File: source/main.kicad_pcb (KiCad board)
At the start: 4 copper layers, 38 x 75 mm, 63 parts, among them J1 pf_533984002, J2 B4B_ZR_SM4_TF, J3 QWIIC, J4 USB_Type_C_Receptacle_14_pin_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, Q1 MOSFET, U1 SCD40, U2 LDO 3.3V ±2% Vin max 4.8V - 5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, U3 LDO 3.3V Vin max 4.8V - 5.2V 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, U4 TXS0102DCUR, U5 BH1750FVI_TR, U6 ESP32_C3_MINI_1, U7 TXS0102DCUR, U8 HLK_LD2410B_P, U9 USB2_0_ESD_Protection

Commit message: Finish trace routing
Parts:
- removed C10, C11, C12, C8, C9: 100nF 16V X7R, lcsc:C0402
- C21, C22, C23, C6, C7: moved to B.Cu
- moved C6 43.9 mm to (0.95, 9.00)
- moved C23 37.0 mm to (0.95, 33.4), turned to 180 degrees
- moved C25 36.0 mm to (-1.75, 25.5), turned to 90 degrees
- moved C22 35.4 mm to (0.95, 27.3), turned to 180 degrees
- moved C21 34.2 mm to (0.95, 21.2), turned to 180 degrees
- moved S1 27.0 mm to (-13.5, 61.5), turned to -90 degrees
- moved S2 27.0 mm to (13.5, 61.5), turned to 90 degrees
- moved LED4 12.2 mm to (0.00, 29.3)
- moved C7 11.7 mm to (0.95, 15.1), turned to 180 degrees
- moved LED3 6.10 mm to (0.00, 23.2)
- moved LED2 6.10 mm to (0.00, 17.1)
- moved C2 5.53 mm to (0.15, 64.5), turned to -90 degrees
- moved C4 5.53 mm to (6.15, 64.5), turned to -90 degrees
- moved R3 5.47 mm to (-1.86, 5.50), turned to 180 degrees
- moved R4 5.47 mm to (-1.86, 8.50), turned to 180 degrees
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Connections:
- net S1-1-S1-2-U6-8 renamed CHIP_EN
- J4 pad 12: J4-12-R8-1 -> USB_CC1
- J4 pad 5: J4-5-R9-1 -> USB_CC2
- Q1 pad 1: MCU_GPIO7 -> MCU_GPIO4
- R5 pad 1: MCU_GPIO7 -> MCU_GPIO4
- R8 pad 1: J4-12-R8-1 -> USB_CC2
- R9 pad 1: J4-5-R9-1 -> USB_CC1
- U2 pad 3: U2-3-U3-3 -> 5V
- U3 pad 3: U2-3-U3-3 -> 5V
- U6 pad 21: MCU_GPIO7 -> DSF_MCU_UART1_TX
- U6 pad 22: MCU_GPIO8 -> DSF_MCU_UART1_RX
- U6 pad 26: MCU_GPIO18 -> USB_DN
- U6 pad 27: MCU_GPIO19 -> USB_DP
- U6 pad 30: U6-30 -> DSF_MCU_UART0_RX
- U6 pad 31: U6-31 -> DSF_MCU_UART0_TX
- U6 pad 5: MCU_GPIO2 -> SCL
- U6 pad 6: MCU_GPIO3 -> SDA
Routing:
- net 5V: track 12.9 -> 176.8 mm, vias 5 -> 12
- net 3V3_PERIPHERAL: track 11.6 -> 118.6 mm, vias 0 -> 7
- net DSF_MCU_UART0_RX: track 0.00 -> 76.6 mm, vias 0 -> 1
- net DSF_MCU_UART0_TX: track 0.00 -> 69.1 mm, vias 0 -> 1
- net MCU_GPIO9: track 0.00 -> 66.0 mm, vias 0 -> 2
- net MCU_GPIO6: track 0.00 -> 61.9 mm, vias 0 -> 1
- net 3V3_MCU: track 1.50 -> 53.1 mm, vias 0 -> 2
- net CHIP_EN: track 0.00 -> 47.5 mm
- net SCL: track 16.1 -> 51.9 mm, vias 2 -> 4
- net MCU_GPIO4: track 0.00 -> 35.3 mm, vias 0 -> 2
- net GND: track 2.19 -> 37.4 mm
- net SDA: track 17.4 -> 52.2 mm, vias 2 -> 3
- net USF_PM_SENSOR_LEVEL_SHIFTER_RX: track 0.00 -> 33.6 mm, vias 0 -> 2
- net USF_PM_SENSOR_LEVEL_SHIFTER_TX: track 0.00 -> 28.7 mm, vias 0 -> 2
- net MCU_GPIO5: track 0.00 -> 23.5 mm, vias 0 -> 3
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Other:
- board text added: "######"
- board text added: "07d9974"
- board text removed: "842de74"

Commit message: genral fixes and improvements
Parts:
- removed H1, H2, H3: Mounting_Hole, MountingHole:MountingHole_3.2mm_M3_Pad
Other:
- board text added: "ddad8a3"
- board text removed: "07d9974"

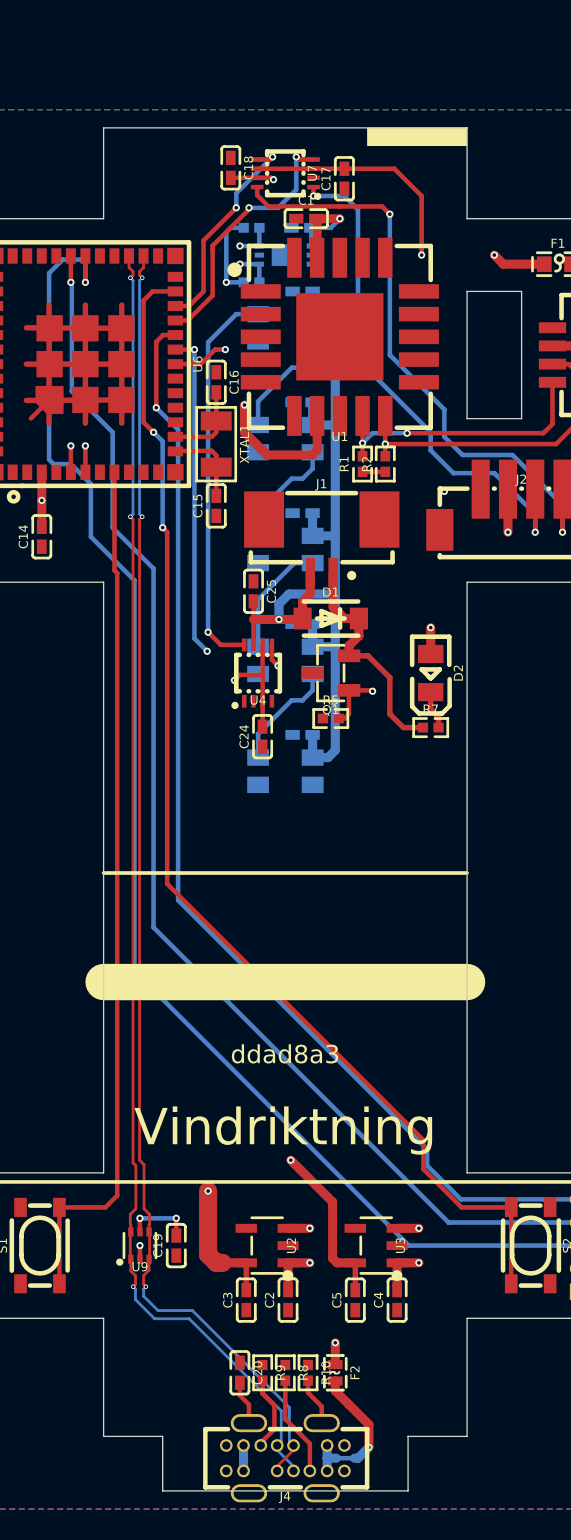
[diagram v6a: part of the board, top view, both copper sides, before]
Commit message: Fix holes
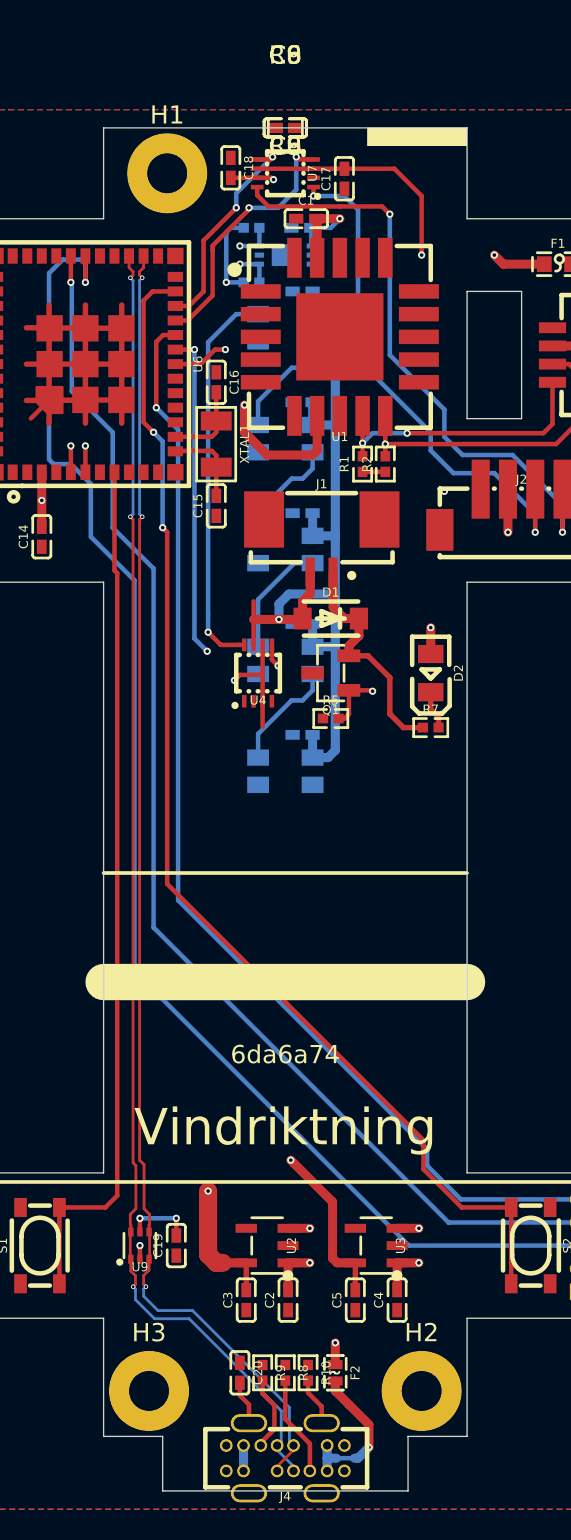
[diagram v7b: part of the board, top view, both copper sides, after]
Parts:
- removed C24, C25: 100nF 16V X7R, lcsc:C0402
- added C8, C9: 100nF 16V X7R, lcsc:C0402, F.Cu at (0.00, 0.00)
- added H1: Mounting_Hole, MountingHole:MountingHole_2.2mm_M2_Pad, F.Cu at (-6.50, 2.50)
- added H2: Mounting_Hole, MountingHole:MountingHole_2.2mm_M2_Pad, F.Cu at (7.50, 69.5)
- added H3: Mounting_Hole, MountingHole:MountingHole_2.2mm_M2_Pad, F.Cu at (-7.50, 69.5)
- added R6: 100Ω, lcsc:R0402, F.Cu at (0.00, 0.00)
- U2: value LDO 3.3V ±2% Vin max 4.8V - 5.2V Iq -> LDO 3.3V ±2% Vin max 4.8V - 5.2V Iq
- U3: value LDO 3.3V Vin max 4.8V - 5.2V Iq -> LDO 3.3V Vin max 4.8V - 5.2V Iq
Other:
- board text added: "6da6a74"
- board text removed: "ddad8a3"

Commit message: Rerun
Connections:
- R8 pad 1: USB_CC2 -> USB_CC1
- R9 pad 1: USB_CC1 -> USB_CC2
- U2 pad 3: 5V -> U2-3-U3-3
- U3 pad 3: 5V -> U2-3-U3-3
- U6 pad 21: DSF_MCU_UART1_TX -> U6-21
- U6 pad 22: DSF_MCU_UART1_RX -> U6-22
- U6 pad 26: USB_DN -> U6-26
- U6 pad 27: USB_DP -> U6-27
- U6 pad 30: DSF_MCU_UART0_RX -> U6-30
- U6 pad 31: DSF_MCU_UART0_TX -> U6-31
- U6 pad 5: SCL -> U6-5
- U6 pad 6: SDA -> U6-6
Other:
- board text added: "d4608c1"
- board text removed: "6da6a74"
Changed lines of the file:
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@@
             (layers "F.Cu" "F.Paste" "F.Mask")
             (remove_unused_layers no)
-            (net 7 "SCL")
+            (net 80 "U6-5")
 )
         (pad "6" smd rect
@@
             (layers "F.Cu" "F.Paste" "F.Mask")
             (remove_unused_layers no)
-            (net 1 "SDA")
+            (net 84 "U6-6")
 )
         (pad "7" smd rect
@@
             (layers "F.Cu" "F.Paste" "F.Mask")
             (remove_unused_layers no)
-            (net 32 "DSF_MCU_UART1_TX")
+            (net 82 "U6-21")
 )
         (pad "22" smd rect
@@
             (layers "F.Cu" "F.Paste" "F.Mask")
             (remove_unused_layers no)
-            (net 31 "DSF_MCU_UART1_RX")
+            (net 86 "U6-22")
 )
         (pad "23" smd rect
@@
             (layers "F.Cu" "F.Paste" "F.Mask")
             (remove_unused_layers no)
-            (net 42 "USB_DN")
+            (net 81 "U6-26")
 )
         (pad "27" smd rect
@@
             (layers "F.Cu" "F.Paste" "F.Mask")
             (remove_unused_layers no)
-            (net 43 "USB_DP")
+            (net 78 "U6-27")
 )
         (pad "28" smd rect
@@
             (layers "F.Cu" "F.Paste" "F.Mask")
             (remove_unused_layers no)
-            (net 77 "DSF_MCU_UART0_RX")
+            (net 79 "U6-30")
 )
         (pad "31" smd rect
@@
             (layers "F.Cu" "F.Paste" "F.Mask")
             (remove_unused_layers no)
-            (net 48 "DSF_MCU_UART0_TX")
+            (net 83 "U6-31")
 )
         (pad "32" smd rect
@@
             (layers "F.Cu" "F.Paste" "F.Mask")
             (remove_unused_layers no)
-            (net 44 "USB_CC2")
+            (net 39 "USB_CC1")
 )
         (pad "2" smd rect
@@
             (layers "F.Cu" "F.Paste" "F.Mask")
             (remove_unused_layers no)
-            (net 35 "5V")
+            (net 85 "U2-3-U3-3")
 )
         (pad "4" smd rect
@@
             (layers "F.Cu" "F.Paste" "F.Mask")
             (remove_unused_layers no)
-            (net 39 "USB_CC1")
+            (net 44 "USB_CC2")
 )
         (pad "2" smd rect
@@
             (layers "F.Cu" "F.Paste" "F.Mask")
             (remove_unused_layers no)
-            (net 35 "5V")
+            (net 85 "U2-3-U3-3")
 )
         (pad "4" smd rect
@@
                 (thickness 0.15))
             (justify )))
-    (gr_text "6da6a74"
+    (gr_text "d4608c1"
         (at 0 51 0)
         (layer "F.SilkS")
